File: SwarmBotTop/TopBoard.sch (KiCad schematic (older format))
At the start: 22 parts, among them IC1 ESP32-PICO-D4, J1 Conn_01x04_Female, J2 Conn_01x04_Female, J3 Conn_01x04_Female, SW1 SW_Push_Open, SW2 SW_Push_Open

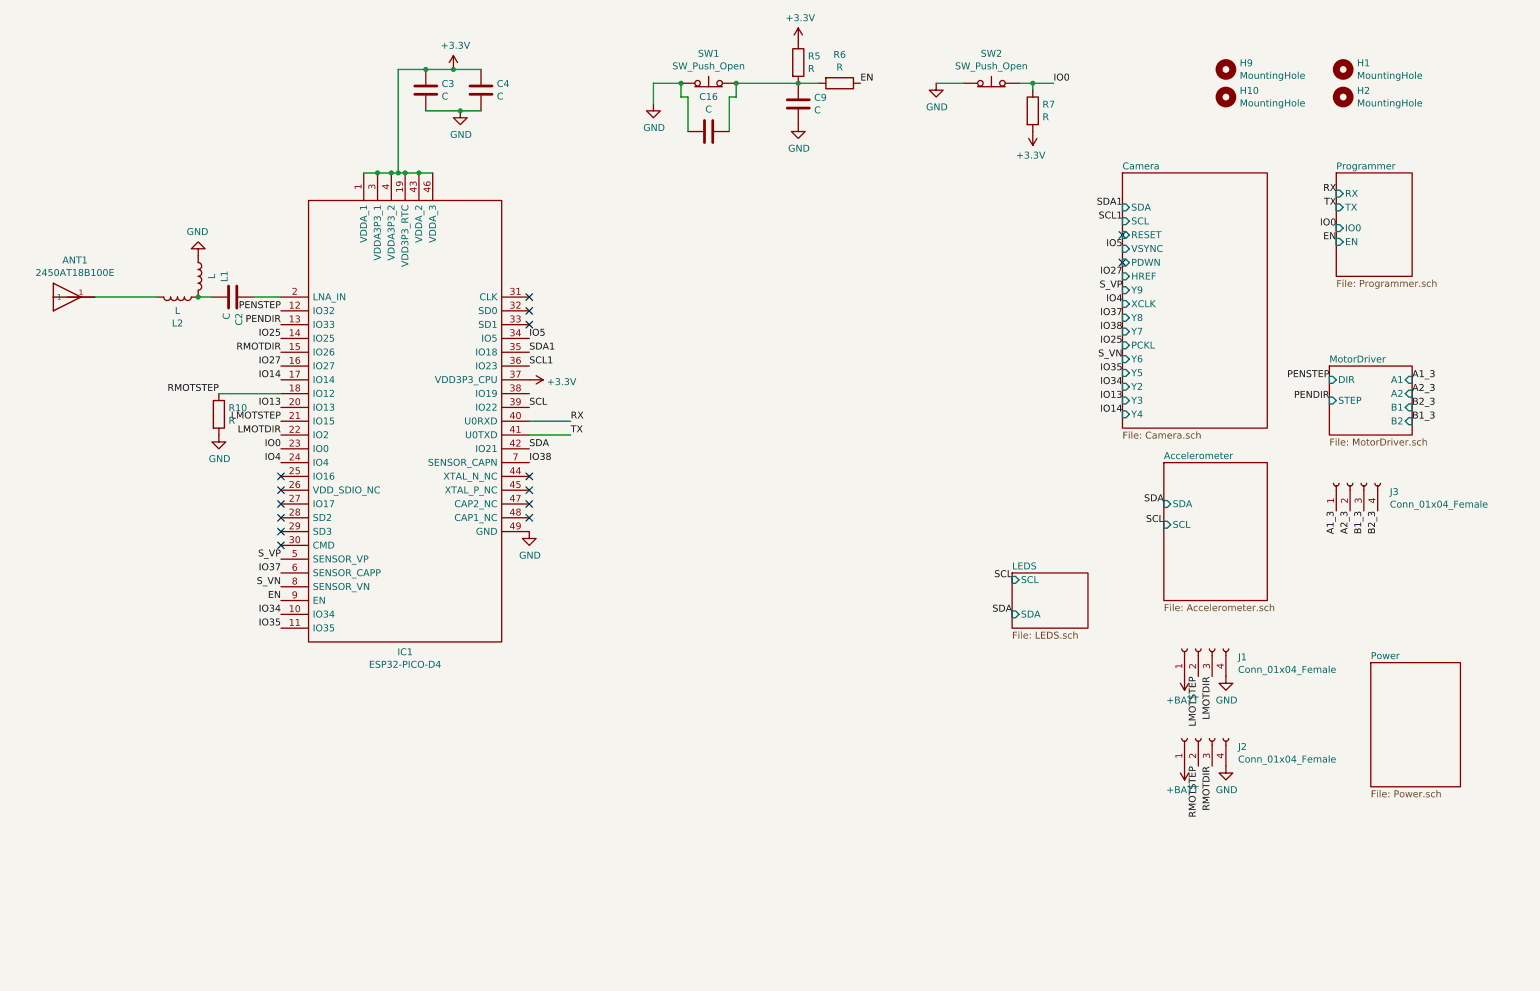
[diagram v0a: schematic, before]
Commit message: Camera routing with all sensors and motors
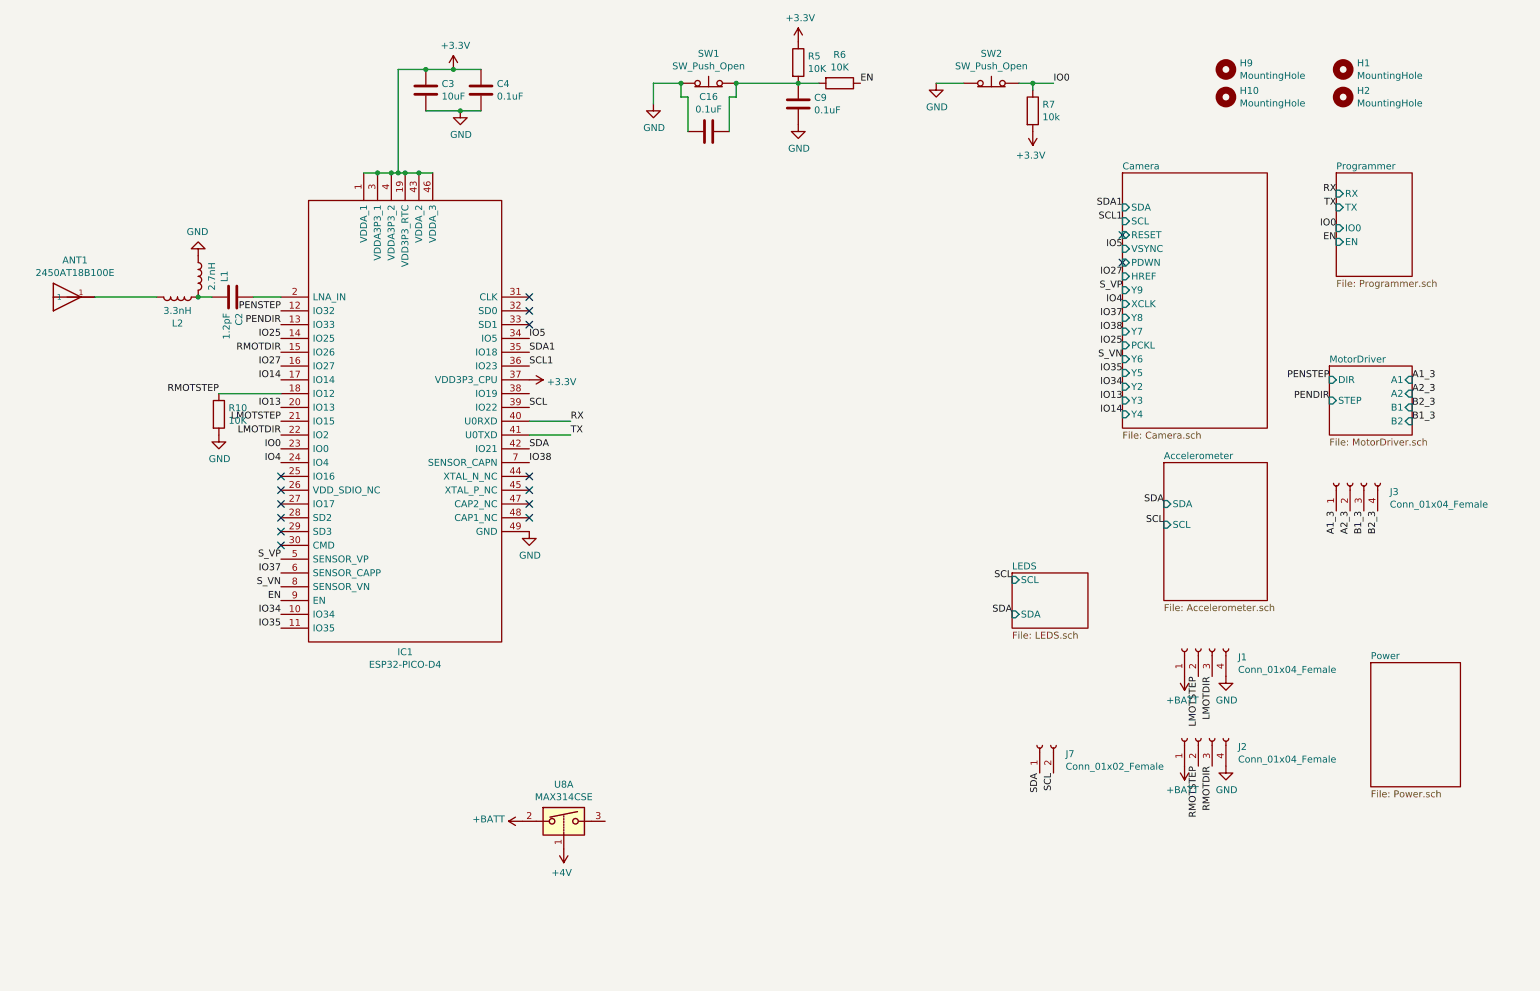
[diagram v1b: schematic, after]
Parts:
- added J7: Conn_01x02_Female, Connector_PinSocket_2.54mm:PinSocket_1x02_P2.54mm_Vertical_SMD_Pin1Left, symbol Connector:Conn_01x02_Female
- added U8: MAX314CSE, switch:K3-1296S-E1, symbol Analog_Switch:MAX314CSE
- C16, C4, C9: value C -> 0.1uF
- C2: value C -> 1.2pF
- C3: value C -> 10uF
- L1: value L -> 2.7nH
- L2: value L -> 3.3nH
- R10, R5, R6: value R -> 10K
- R7: value R -> 10k
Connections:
- net +BATT: now also U8.2
- net SCL: now also J7.2 (Pin_2)
- net SDA: now also J7.1 (Pin_1)
- new net +4V: U8.1
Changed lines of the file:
@@
 P 3300 1100
 F 0 "C3" H 3415 1146 50  0000 L CNN
-F 1 "C" H 3415 1055 50  0000 L CNN
+F 1 "10uF" H 3415 1055 50  0000 L CNN
 F 2 "Capacitor_SMD:C_0402_1005Metric" H 3338 950 50  0001 C CNN
 F 3 "~" H 3300 1100 50  0001 C CNN
@@
 P 3700 1100
 F 0 "C4" H 3815 1146 50  0000 L CNN
-F 1 "C" H 3815 1055 50  0000 L CNN
+F 1 "0.1uF" H 3815 1055 50  0000 L CNN
 F 2 "Capacitor_SMD:C_0402_1005Metric" H 3738 950 50  0001 C CNN
 F 3 "~" H 3700 1100 50  0001 C CNN
@@
 P 1900 2600
 F 0 "C2" H 2015 2646 50  0000 L CNN
-F 1 "C" H 2015 2555 50  0000 L CNN
+F 1 "1.2pF" H 2015 2555 50  0000 L CNN
 F 2 "Capacitor_SMD:C_0402_1005Metric" H 1938 2450 50  0001 C CNN
 F 3 "~" H 1900 2600 50  0001 C CNN
@@
 P 1650 2450
 F 0 "L1" V 1840 2450 50  0000 C CNN
-F 1 "L" V 1749 2450 50  0000 C CNN
+F 1 "2.7nH" V 1749 2450 50  0000 C CNN
 F 2 "Inductor_SMD:L_0402_1005Metric" H 1650 2450 50  0001 C CNN
 F 3 "~" H 1650 2450 50  0001 C CNN
@@
 P 6000 1200
 F 0 "C9" H 6115 1246 50  0000 L CNN
-F 1 "C" H 6115 1155 50  0000 L CNN
+F 1 "0.1uF" H 6115 1155 50  0000 L CNN
 F 2 "Capacitor_SMD:C_0402_1005Metric" H 6038 1050 50  0001 C CNN
 F 3 "~" H 6000 1200 50  0001 C CNN
@@
 P 6000 900
 F 0 "R5" H 6070 946 50  0000 L CNN
-F 1 "R" H 6070 855 50  0000 L CNN
+F 1 "10K" H 6070 855 50  0000 L CNN
 F 2 "Resistor_SMD:R_0402_1005Metric" V 5930 900 50  0001 C CNN
 F 3 "~" H 6000 900 50  0001 C CNN
@@
 P 6300 1050
 F 0 "R6" V 6093 1050 50  0000 C CNN
-F 1 "R" V 6184 1050 50  0000 C CNN
+F 1 "10K" V 6184 1050 50  0000 C CNN
 F 2 "Resistor_SMD:R_0402_1005Metric" V 6230 1050 50  0001 C CNN
 F 3 "~" H 6300 1050 50  0001 C CNN
@@
 P 7700 1250
 F 0 "R7" H 7770 1296 50  0000 L CNN
-F 1 "R" H 7770 1205 50  0000 L CNN
+F 1 "10k" H 7770 1205 50  0000 L CNN
 F 2 "Resistor_SMD:R_0402_1005Metric" V 7630 1250 50  0001 C CNN
 F 3 "~" H 7700 1250 50  0001 C CNN
@@
 P 5350 1400
 F 0 "C16" V 5098 1400 50  0000 C CNN
-F 1 "C" V 5189 1400 50  0000 C CNN
+F 1 "0.1uF" V 5189 1400 50  0000 C CNN
 F 2 "Capacitor_SMD:C_0402_1005Metric" H 5388 1250 50  0001 C CNN
 F 3 "~" H 5350 1400 50  0001 C CNN
@@
 P 1800 3450
 F 0 "R10" H 1870 3496 50  0000 L CNN
-F 1 "R" H 1870 3405 50  0000 L CNN
+F 1 "10K" H 1870 3405 50  0000 L CNN
 F 2 "Resistor_SMD:R_0402_1005Metric" V 1730 3450 50  0001 C CNN
 F 3 "~" H 1800 3450 50  0001 C CNN
@@
 P 1500 2600
 F 0 "L2" V 1690 2600 50  0000 C CNN
-F 1 "L" V 1599 2600 50  0000 C CNN
+F 1 "3.3nH" V 1599 2600 50  0000 C CNN
 F 2 "Inductor_SMD:L_0402_1005Metric" H 1500 2600 50  0001 C CNN
 F 3 "~" H 1500 2600 50  0001 C CNN
@@
 Text Label 4050 3000 0    50   ~ 0
 SDA1
+$Comp
+L Connector:Conn_01x02_Female J7
+U 1 1 5DF82F9B
+P 7750 5850
+F 0 "J7" V 7688 5662 50  0000 R CNN
+F 1 "Conn_01x02_Female" V 7597 5662 50  0000 R CNN
+F 2 "Connector_PinSocket_2.54mm:PinSocket_1x02_P2.54mm_Vertical_SMD_Pin1Left" H 7750 5850 50  0001 C CNN
+F 3 "~" H 7750 5850 50  0001 C CNN
+	1    7750 5850
+	0    -1   -1   0
+$EndComp
+Text Label 7750 6050 3    50   ~ 0
+SDA
+Text Label 7850 6050 3    50   ~ 0
+SCL
+$Comp
+L Analog_Switch:MAX314CSE U8
+U 1 1 5DF8E978
+P 4300 6400
+F 0 "U8" H 4300 6667 50  0000 C CNN
+F 1 "MAX314CSE" H 4300 6576 50  0000 C CNN
+F 2 "switch:K3-1296S-E1" H 4300 6300 50  0001 C CNN
+F 3 "https://datasheets.maximintegrated.com/en/ds/MAX312-MAX314.pdf" H 4300 6400 50  0001 C CNN
+	1    4300 6400
+	1    0    0    -1
+$EndComp
+$Comp
+L power:+BATT #PWR0152
+U 1 1 5DF905DE
+P 4000 6400
+F 0 "#PWR0152" H 4000 6250 50  0001 C CNN
+F 1 "+BATT" V 4015 6527 50  0000 L CNN
+F 2 "" H 4000 6400 50  0001 C CNN
+F 3 "" H 4000 6400 50  0001 C CNN
+	1    4000 6400
+	0    -1   -1   0
+$EndComp
+$Comp
+L power:+4V #PWR0188
+U 1 1 5DF908C1
+P 4300 6600
+F 0 "#PWR0188" H 4300 6450 50  0001 C CNN
+F 1 "+4V" H 4315 6773 50  0000 C CNN
+F 2 "" H 4300 6600 50  0001 C CNN
+F 3 "" H 4300 6600 50  0001 C CNN
+	1    4300 6600
+	-1   0    0    1
+$EndComp
 $EndSCHEMATC

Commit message: things
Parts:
- removed H9: MountingHole, MountingHole:MountingHole_2.5mm, symbol Mechanical:MountingHole
- added H3: MountingHole_Pad, MountingHole:MountingHole_2.5mm_Pad, symbol Mechanical:MountingHole_Pad
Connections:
- net PENSTEP: now also IC1.38 (IO19); no longer IC1.12 (IO32)
- new net CAPTOUCH: H3.1, IC1.12 (IO32)
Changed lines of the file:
@@
-$EndComp
-$Comp
-L Mechanical:MountingHole H9
-U 1 1 5DB371B3
-P 9100 950
-F 0 "H9" H 9200 996 50  0000 L CNN
-F 1 "MountingHole" H 9200 905 50  0000 L CNN
-F 2 "MountingHole:MountingHole_2.5mm" H 9100 950 50  0001 C CNN
-F 3 "~" H 9100 950 50  0001 C CNN
-	1    9100 950
-	1    0    0    -1
 $EndComp
 $Comp
@@
 Text Label 2250 3000 2    50   ~ 0
 RMOTDIR
-Text Label 2250 2700 2    50   ~ 0
+Text Label 4050 3300 0    50   ~ 0
 PENSTEP
 Text Label 2250 2800 2    50   ~ 0
@@
 	-1   0    0    1
 $EndComp
+Text Label 2250 2700 2    50   ~ 0
+CAPTOUCH
+$Comp
+L Mechanical:MountingHole_Pad H3
+U 1 1 5E02FF33
+P 9100 900
+F 0 "H3" H 9200 949 50  0000 L CNN
+F 1 "MountingHole_Pad" H 9200 858 50  0000 L CNN
+F 2 "MountingHole:MountingHole_2.5mm_Pad" H 9100 900 50  0001 C CNN
+F 3 "~" H 9100 900 50  0001 C CNN
+	1    9100 900
+	1    0    0    -1
+$EndComp
+Text Label 9100 1000 2    50   ~ 0
+CAPTOUCH
 $EndSCHEMATC

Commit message: Final Design
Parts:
- removed IC1: ESP32-PICO-D4, ESP32-PICO-D4:ESP32-PICO-D4_1, symbol SwarmBot-rescue:ESP32-PICO-D4-ESP32-PICO-D4
- removed L1: 2.7nH, Inductor_SMD:L_0402_1005Metric, symbol Device:L
- removed L2: 3.3nH, Inductor_SMD:L_0402_1005Metric, symbol Device:L
- removed R10: 10K, Resistor_SMD:R_0402_1005Metric, symbol Device:R
- removed R7: 10k, Resistor_SMD:R_0402_1005Metric, symbol Device:R
- removed SW2: SW_Push_Open, Button_Switch_SMD:SW_SPST_CK_KXT3, symbol Switch:SW_Push_Open
- added C23: 1uF, Capacitor_SMD:C_0402_1005Metric, symbol Device:C
- added C5: 3.3nF, Capacitor_SMD:C_0402_1005Metric, symbol Device:C
- added C7: 12Pf, Capacitor_SMD:C_0402_1005Metric, symbol Device:C
- added C8: 12pF, Capacitor_SMD:C_0402_1005Metric, symbol Device:C
- added D4: LED, LED_SMD:LED_0603_1608Metric, symbol Device:LED
- added R22, R3, R9: 10K, Resistor_SMD:R_0402_1005Metric, symbol Device:R
- added TP1, TP2, TP3, TP4: TestPoint, TestPoint:TestPoint_Pad_D1.0mm, symbol Connector:TestPoint
- added U1: ESP32-D0WD, footprints:ESP32-D0WD, symbol 2020-04-14_02-24-10:ESP32-D0WD
- added Y1: 40MHz, Crystal:Crystal_SMD_2520-4Pin_2.5x2.0mm, symbol Device:Crystal_GND24_Small
- C2: value 1.2pF -> 0.1uF
- C3: value 10uF -> 0.1uF
- C9: value 0.1uF -> 10nF
- J1, J2: footprint Connector_PinHeader_2.54mm:PinHeader_1x04_P2.54mm_Vertical_SMD_Pin1Left -> Connector_PinHeader_2.54mm:PinHeader_1x04_P2.54mm_Vertical_SMD_Pin1Right
- J7: footprint Connector_PinSocket_2.54mm:PinSocket_1x02_P2.54mm_Vertical_SMD_Pin1Left -> Connector_PinSocket_2.54mm:PinSocket_1x02_P2.54mm_Vertical_SMD_Pin1Right
- R6: value 10K -> 20K
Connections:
- net +3V3: now also C2.2, C3.2, C4.2, R22.1, R3.2, U1.1 (VDDA), U1.19 (VDD3P3_RTC), U1.3 (VDD3P3), U1.37 (VDD3P3_CPU), U1.4 (VDD3P3), U1.43 (VDDA), U1.46 (VDDA); no longer C3.1, C4.1
- net +BATT: now also R9.2
- net CAPTOUCH: now also U1.12 (32K_XP)
- net EN: now also C16.1, R5.2, SW1.2 (B), C23.2, TP4.1, U1.9 (CHIP_PU); no longer R6.1
- net GND: now also C2.1, C3.1, C4.1, C9.1, C23.1, C7.1, C8.1, D4.1 (K), U1.49 (GND), Y1.1, Y1.3; no longer C3.2, C4.2, C9.2
- net IO0: now also TP3.1, U1.23 (GPIO0)
- net IO13: now also U1.20 (MTCK)
- net IO14: now also U1.17 (MTMS)
- net IO25: now also U1.14 (GPIO25)
- net IO27: now also U1.16 (GPIO27)
- net IO34: now also U1.10 (VDET_1)
- net IO35: now also U1.11 (VDET_2)
- net IO37: now also U1.6 (SENSOR_CAPP)
- net IO38: now also U1.7 (SENSOR_CAPN)
- net IO4: now also U1.24 (GPIO4)
- net LMOTDIR: now also U1.22 (GPIO2)
- net LMOTSTEP: now also U1.21 (MTDO)
- net RMOTDIR: now also U1.13 (32K_XN)
- net RMOTSTEP: now also U1.15 (GPIO26)
- net RX: now also TP1.1, U1.40 (U0RXD)
- net SCL: now also U1.39 (GPIO22)
- net SCL1: now also U1.36 (GPIO23)
- net SDA: now also U1.42 (GPIO21)
- net SDA1: now also U1.35 (GPIO18)
- net S_VN: now also U1.8 (SENSOR_VN)
- net S_VP: now also U1.5 (SENSOR_VP)
- net TX: now also TP2.1, U1.41 (U0TXD)
- net at ANT1.1: now also U1.2 (LNA_IN)
- new net: D4.2 (A), R9.1
- new net: R3.1, U1.18 (MTDI)
- new net: C8.2, U1.44 (XTAL_N), Y1.2
- new net: C7.2, U1.45 (XTAL_P), Y1.4
- new net: C5.2, R6.2, U1.47 (CAP2)
- new net: C5.1, C9.2, R6.1, U1.48 (CAP1)
- new net CMD: U1.30 (SD_CMD)
- new net IO16: U1.25 (GPIO16)
- new net IO17: U1.27 (GPIO17)
- new net LIO5: U1.34 (GPIO5)
- new net SD0: U1.32 (SD_DATA_0)
- new net SD1: U1.33 (SD_DATA_1)
- new net SD2: U1.28 (SD_DATA_2)
- new net SD3: R22.2, U1.29 (SD_DATA_3)
- new net SD_SLC: U1.31 (SD_CLK)
- new net VDD_SDIO: U1.26 (VDD_SDIO)
- no-connect marks 15 -> 2
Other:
- moved on the sheet: ANT1, U8A
